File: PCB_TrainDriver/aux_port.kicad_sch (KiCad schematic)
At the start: 15 parts, among them J3 aux_port1, J4 aux_port2, J5 aux_port3, Q10 BSC014N04LS, Q11 BSC014N04LS, Q9 BSC014N04LS

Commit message: Update_main_PCB
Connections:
- net aux_port1 renamed Pneumatic
- net aux_port2 renamed Horn
- net aux_port3 renamed Lamp
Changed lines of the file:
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@@
 		)
 	)
-	(hierarchical_label "aux_port2"
+	(hierarchical_label "Horn"
 		(shape input)
 		(at 134.62 87.63 180)
@@
 		)
 	)
-	(hierarchical_label "aux_port3"
+	(hierarchical_label "Lamp"
 		(shape input)
 		(at 214.63 87.63 180)
@@
 		)
 	)
-	(hierarchical_label "aux_port1"
+	(hierarchical_label "Pneumatic"
 		(shape input)
 		(at 55.88 86.36 180)
@@
 			)
 		)
+		(property "JLCPCB Part #" ""
+			(at 95.25 77.47 0)
+			(hide yes)
+			(show_name no)
+			(do_not_autoplace no)
+			(effects
+				(font
+					(size 1.27 1.27)
+				)
+			)
+		)
 		(pin "1"
 		)
@@
 			)
 		)
+		(property "JLCPCB Part #" ""
+			(at 171.45 90.17 0)
+			(hide yes)
+			(show_name no)
+			(do_not_autoplace no)
+			(effects
+				(font
+					(size 1.27 1.27)
+				)
+			)
+		)
 		(pin "4"
 		)
@@
 			)
 		)
+		(property "JLCPCB Part #" ""
+			(at 147.32 87.63 90)
+			(hide yes)
+			(show_name no)
+			(do_not_autoplace no)
+			(effects
+				(font
+					(size 1.27 1.27)
+				)
+			)
+		)
 		(pin "1"
 		)
@@
 				(font
 					(size 0.889 0.889)
+				)
+			)
+		)
+		(property "JLCPCB Part #" ""
+			(at 151.13 93.98 0)
+			(hide yes)
+			(show_name no)
+			(do_not_autoplace no)
+			(effects
+				(font
+					(size 1.27 1.27)
 				)
 			)
@@
 			)
 		)
+		(property "JLCPCB Part #" ""
+			(at 158.75 76.2 90)
+			(hide yes)
+			(show_name no)
+			(do_not_autoplace no)
+			(effects
+				(font
+					(size 1.27 1.27)
+				)
+			)
+		)
 		(pin "1"
 		)
@@
 			)
 		)
+		(property "JLCPCB Part #" ""
+			(at 80.01 74.93 90)
+			(hide yes)
+			(show_name no)
+			(do_not_autoplace no)
+			(effects
+				(font
+					(size 1.27 1.27)
+				)
+			)
+		)
 		(pin "1"
 		)
@@
 			)
 		)
+		(property "JLCPCB Part #" ""
+			(at 254 78.74 0)
+			(hide yes)
+			(show_name no)
+			(do_not_autoplace no)
+			(effects
+				(font
+					(size 1.27 1.27)
+				)
+			)
+		)
 		(pin "1"
 		)
@@
 			)
 		)
+		(property "JLCPCB Part #" ""
+			(at 92.71 88.9 0)
+			(hide yes)
+			(show_name no)
+			(do_not_autoplace no)
+			(effects
+				(font
+					(size 1.27 1.27)
+				)
+			)
+		)
 		(pin "4"
 		)
@@
 			)
 		)
+		(property "JLCPCB Part #" ""
+			(at 72.39 92.71 0)
+			(hide yes)
+			(show_name no)
+			(do_not_autoplace no)
+			(effects
+				(font
+					(size 1.27 1.27)
+				)
+			)
+		)
 		(pin "1"
 		)
@@
 			)
 		)
+		(property "JLCPCB Part #" ""
+			(at 251.46 90.17 0)
+			(hide yes)
+			(show_name no)
+			(do_not_autoplace no)
+			(effects
+				(font
+					(size 1.27 1.27)
+				)
+			)
+		)
 		(pin "4"
 		)
@@
 			)
 		)
+		(property "JLCPCB Part #" ""
+			(at 173.99 78.74 0)
+			(hide yes)
+			(show_name no)
+			(do_not_autoplace no)
+			(effects
+				(font
+					(size 1.27 1.27)
+				)
+			)
+		)
 		(pin "1"
 		)
@@
 			)
 		)
+		(property "JLCPCB Part #" ""
+			(at 238.76 76.2 90)
+			(hide yes)
+			(show_name no)
+			(do_not_autoplace no)
+			(effects
+				(font
+					(size 1.27 1.27)
+				)
+			)
+		)
 		(pin "1"
 		)
@@
 			)
 		)
+		(property "JLCPCB Part #" ""
+			(at 68.58 86.36 90)
+			(hide yes)
+			(show_name no)
+			(do_not_autoplace no)
+			(effects
+				(font
+					(size 1.27 1.27)
+				)
+			)
+		)
 		(pin "1"
 		)
@@
 				(font
 					(size 0.889 0.889)
+				)
+			)
+		)
+		(property "JLCPCB Part #" ""
+			(at 231.14 93.98 0)
+			(hide yes)
+			(show_name no)
+			(do_not_autoplace no)
+			(effects
+				(font
+					(size 1.27 1.27)
 				)
 			)
@@
 				)
 			)
+		)
+		(property "JLCPCB Part #" ""
+			(at 227.33 87.63 90)
+			(hide yes)
+			(show_name no)
+			(do_not_autoplace no)
+			(effects
+				(font
+					(size 1.27 1.27)
+				)
+			)

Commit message: Finished sch
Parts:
- D1, D2, D3: JLCPCB Part # (none) -> C8678
- J3, J4, J5: JLCPCB Part # (none) -> C431092
- Q10, Q11, Q9: JLCPCB Part # (none) -> C2760081
- R10, R12, R7: JLCPCB Part # (none) -> C25804
- R11, R8, R9: JLCPCB Part # (none) -> C23138

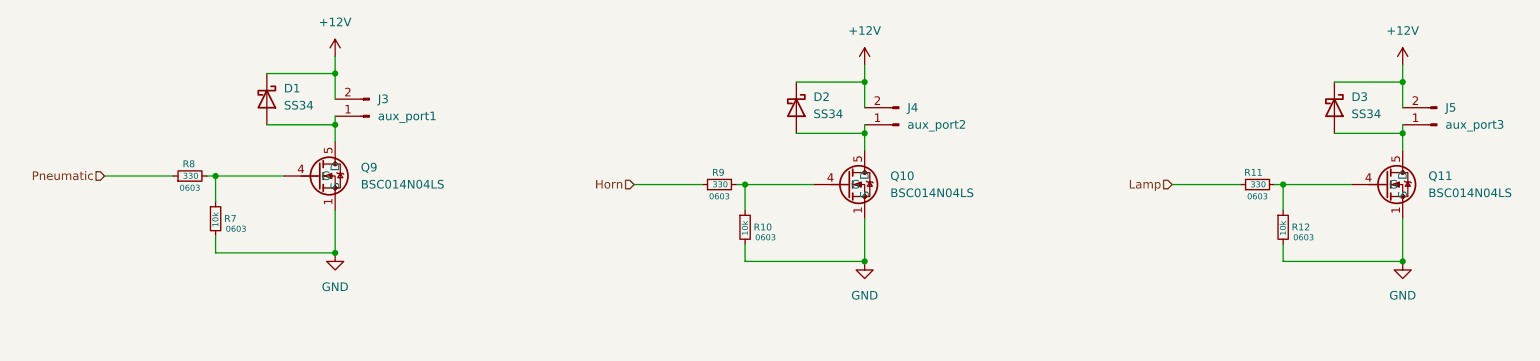
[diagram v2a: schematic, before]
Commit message: Add aux led indicator
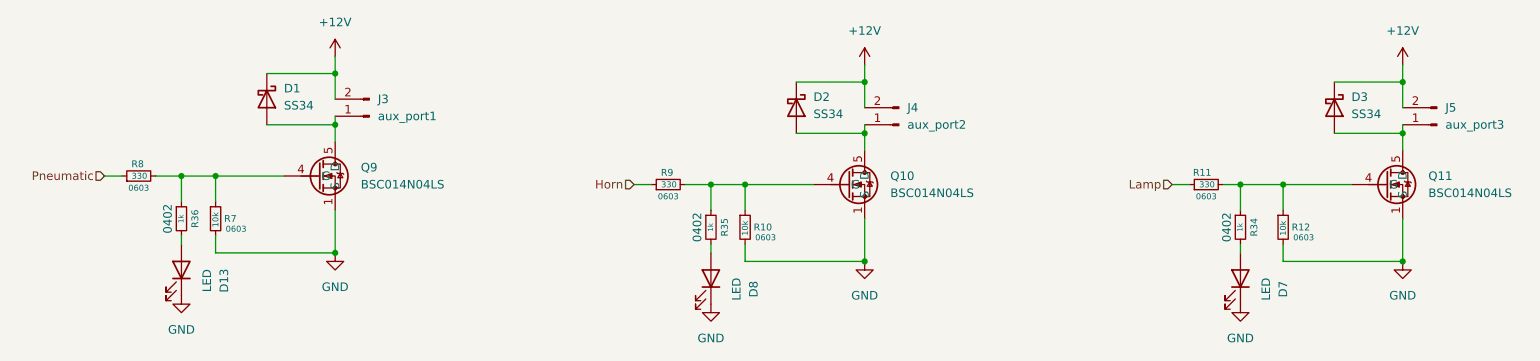
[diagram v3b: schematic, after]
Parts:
- added D13, D7, D8: LED, LED_SMD:LED_0603_1608Metric, symbol Device:LED
- added R34, R35, R36: 1k, Resistor_SMD:R_0402_1005Metric, symbol Device:R_Small
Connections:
- net GND: now also D13.1 (K), D7.1 (K), D8.1 (K)
- net at Q10.4 (G), R10.1, R9.2: now also R35.1
- net at Q9.4 (G), R7.1, R8.2: now also R36.1
- net at Q11.4 (G), R11.2, R12.1: now also R34.1
- new net: D8.2 (A), R35.2
- new net: D7.2 (A), R34.2
- new net: D13.2 (A), R36.2
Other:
- moved on the sheet: R11, R8, R9
